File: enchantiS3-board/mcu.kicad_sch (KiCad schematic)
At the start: 7 parts, among them SW1 BOOT, SW2 ESP_RST

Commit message: Fixed BOM errors, removed unused Mounting Hole, added rev4 BOM
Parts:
- C2: Manufacturer Samsung Electro-Mechanics -> Murata Electronics; Mfg Part # CL05B104KO5NNNC -> GRM155R71C104KA88J
- C9: Manufacturer Samsung Electro-Mechanics -> Murata Electronics; Mfg Part # CL05A105KO5NNNC -> GRM155R61E105KA12D
- R5: Manufacturer Panasonic Electronic Components -> YAGEO; Mfg Part # ERJ-2RKF1002X -> RC0402FR-0710KL
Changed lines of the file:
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@@
 			)
 		)
-		(property "Description" "1 µF ±10% 16V Ceramic Capacitor X5R 0402 (1005 Metric)"
+		(property "Description" "1 µF ±10% 25V Ceramic Capacitor X5R 0402 (1005 Metric)"
 			(at 82.55 49.53 0)
 			(effects
@@
 			)
 		)
-		(property "Mfg Part #" "CL05A105KO5NNNC"
+		(property "Mfg Part #" "GRM155R61E105KA12D"
 			(at 82.55 49.53 0)
 			(effects
@@
 			)
 		)
-		(property "Manufacturer" "Samsung Electro-Mechanics"
+		(property "Manufacturer" "Murata Electronics"
 			(at 82.55 49.53 0)
 			(effects
@@
 			)
 		)
-		(property "Description" "10 kOhms ±1% 0.1W, 1/10W Chip Resistor 0402 (1005 Metric) Automotive AEC-Q200 Thick Film"
+		(property "Description" "10 kOhms ±1%  0.063W, 1/16W Chip Resistor 0402 (1005 Metric)"
 			(at 82.55 38.1 0)
 			(effects
@@
 			)
 		)
-		(property "Mfg Part #" "ERJ-2RKF1002X"
+		(property "Mfg Part #" "RC0402FR-0710KL"
 			(at 82.55 38.1 0)
 			(effects
@@
 			)
 		)
-		(property "Manufacturer" "Panasonic Electronic Components"
+		(property "Manufacturer" "YAGEO"
 			(at 82.55 38.1 0)
 			(effects
@@
 			)
 		)
-		(property "Mfg Part #" "CL05B104KO5NNNC"
+		(property "Mfg Part #" "GRM155R71C104KA88J"
 			(at 63.5 49.53 0)
 			(effects
@@
 			)
 		)
-		(property "Manufacturer" "Samsung Electro-Mechanics"
+		(property "Manufacturer" "Murata Electronics"
 			(at 63.5 49.53 0)
 			(effects

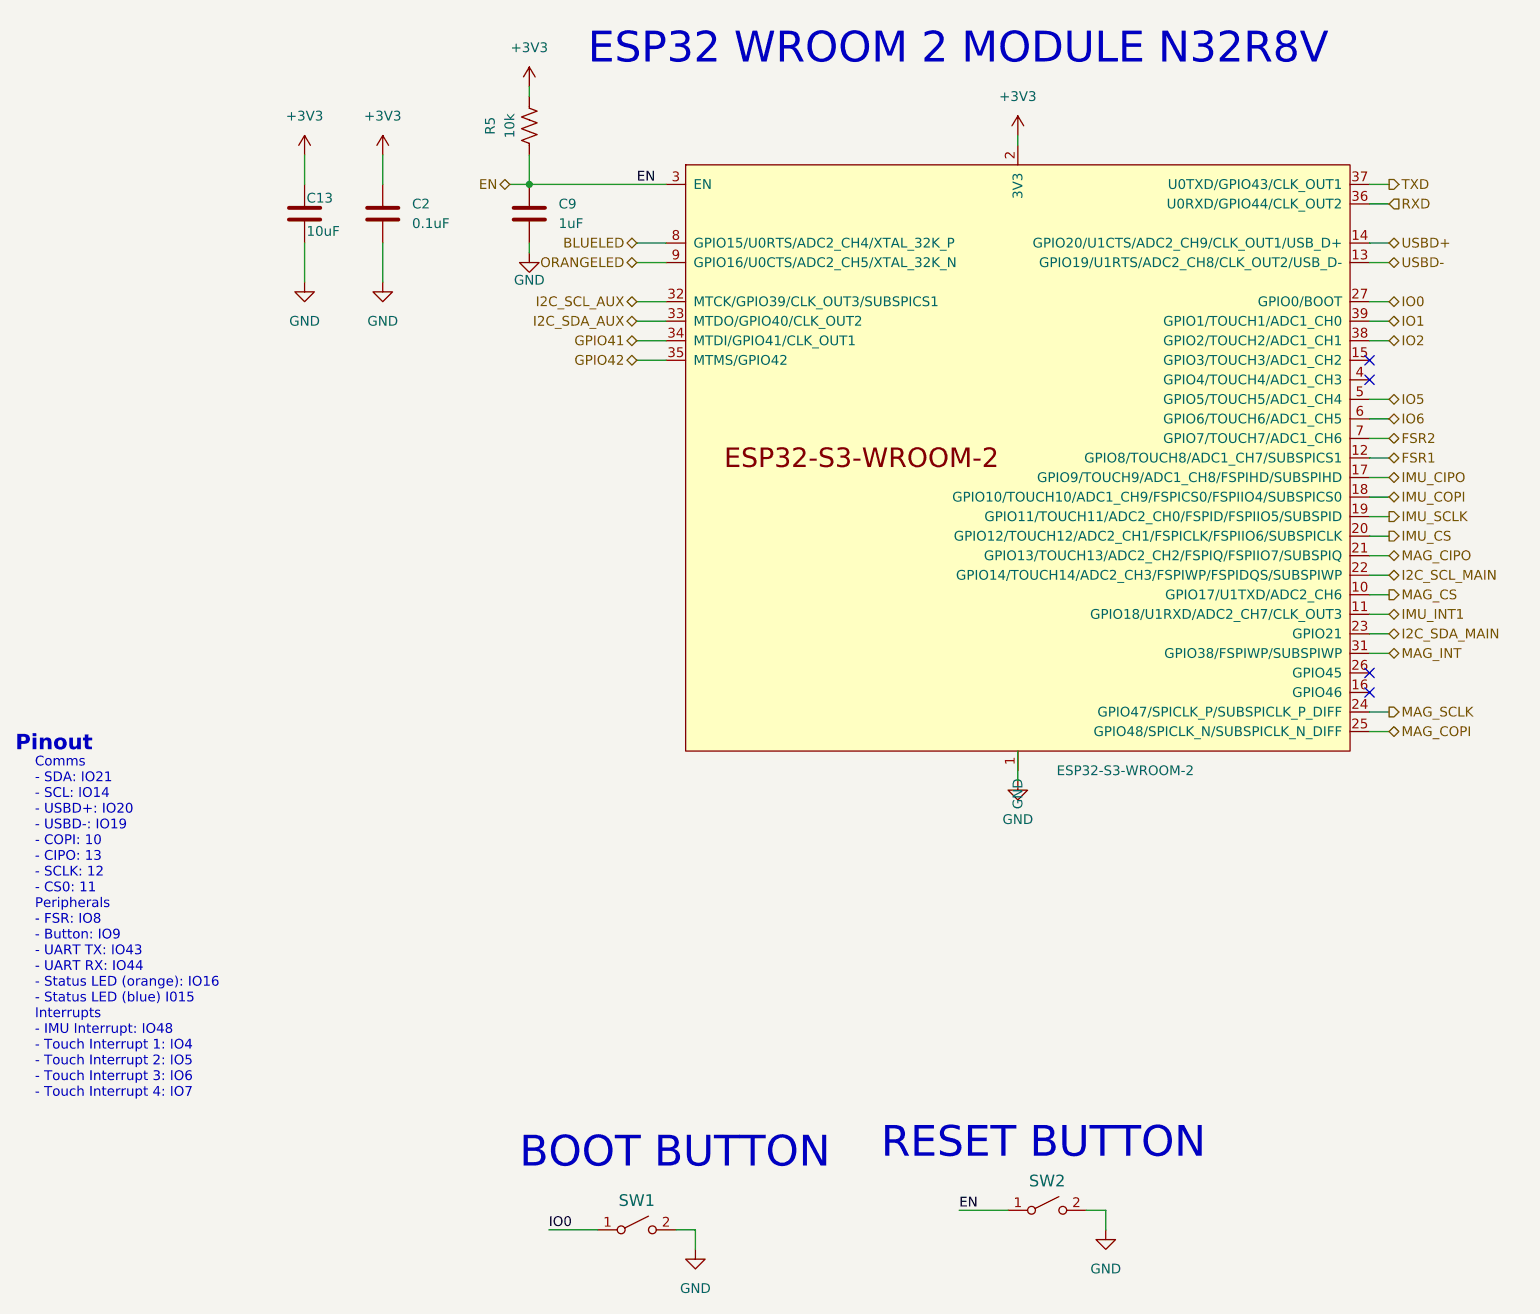
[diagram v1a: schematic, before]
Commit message: Switch to cheaper ESP32S3 WROOM 1 N8R8 Module
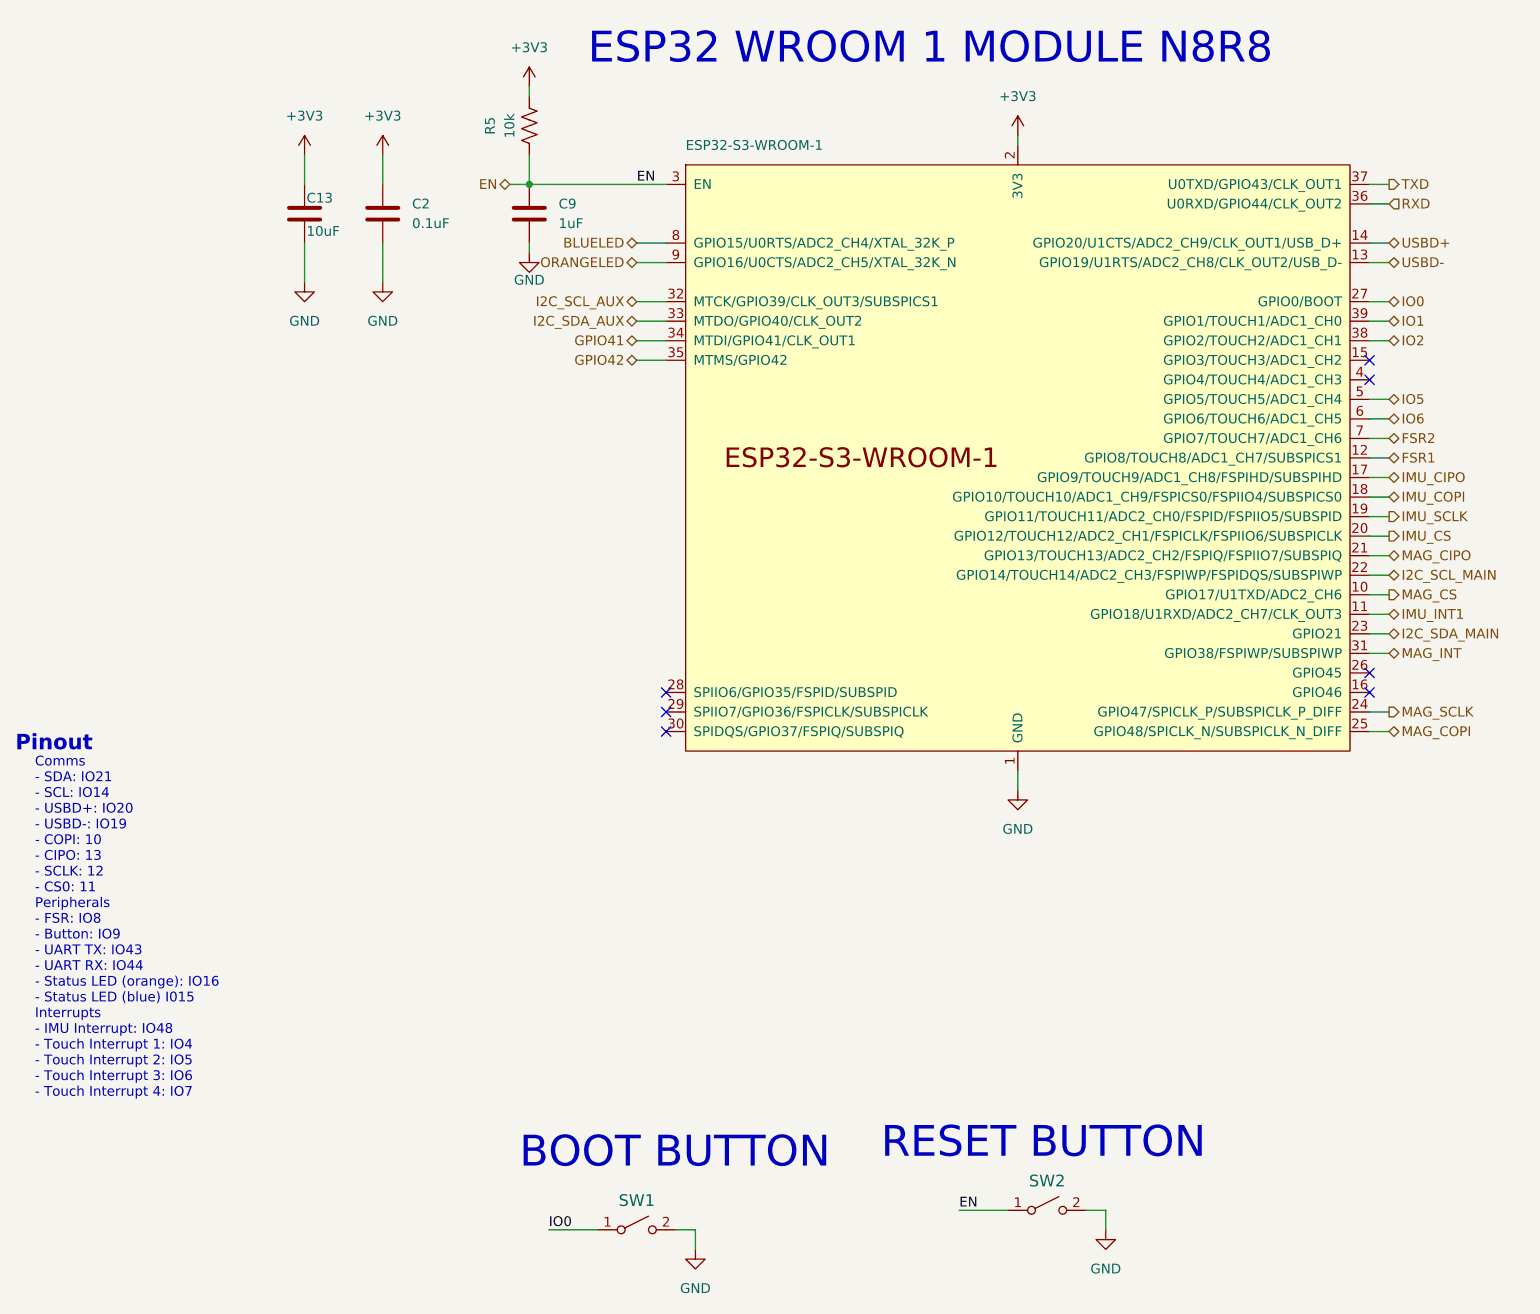
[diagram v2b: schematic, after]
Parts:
- MCU1: value ESP32-S3-WROOM-2 -> ESP32-S3-WROOM-1; footprint PCM_Espressif:ESP32-S3-WROOM-2 -> PCM_Espressif:ESP32-S3-WROOM-1; symbol PCM_Espressif:ESP32-S3-WROOM-2 -> PCM_Espressif:ESP32-S3-WROOM-1; Mfg Part # ESP32-S3-WROOM-2-N32R16V -> ESP32-S3-WROOM-1-N8R8
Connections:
- no-connect marks 4 -> 7
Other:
- note added: "ESP32 WROOM 1 MODULE N8R8"
- note removed: "ESP32 WROOM 2 MODULE N32R8V"
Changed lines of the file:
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@@
 		)
 	)
-	(text "ESP32 WROOM 2 MODULE N32R8V"
+	(text "ESP32 WROOM 1 MODULE N8R8"
 		(exclude_from_sim no)
 		(at 90.17 30.48 0)
@@
 	)
 	(no_connect
+		(at 100.33 114.3)
+	)
+	(no_connect
 		(at 191.77 68.58)
+	)
+	(no_connect
+		(at 100.33 111.76)
 	)
 	(no_connect
@@
 	)
 	(no_connect
+		(at 100.33 116.84)
+	)
+	(no_connect
 		(at 191.77 111.76)
 	)
@@
 	(wire
 		(pts
-			(xy 146.05 119.38) (xy 146.05 123.19)
+			(xy 146.05 121.92) (xy 146.05 124.46)
 		)
 		(stroke
@@
 		(lib_name "GND_2")
 		(lib_id "power:GND")
-		(at 146.05 123.19 0)
+		(at 146.05 124.46 0)
 		(unit 1)
 		(exclude_from_sim no)
@@
 		(fields_autoplaced yes)
 		(property "Reference" "#PWR0101"
+			(at 146.05 130.81 0)
+			(effects
+				(font
+					(size 1.27 1.27)
+				)
+				(hide yes)
+			)
+		)
+		(property "Value" "GND"
 			(at 146.05 129.54 0)
 			(effects
@@
 					(size 1.27 1.27)
 				)
-				(hide yes)
-			)
-		)
-		(property "Value" "GND"
-			(at 146.05 128.27 0)
-			(effects
-				(font
-					(size 1.27 1.27)
-				)
 			)
 		)
 		(property "Footprint" ""
-			(at 146.05 123.19 0)
+			(at 146.05 124.46 0)
 			(effects
 				(font
@@
 		)
 		(property "Datasheet" ""
-			(at 146.05 123.19 0)
+			(at 146.05 124.46 0)
 			(effects
 				(font
@@
 		)
 		(property "Description" ""
-			(at 146.05 123.19 0)
+			(at 146.05 124.46 0)
 			(effects
 				(font
@@
 	)
 	(symbol
-		(lib_id "PCM_Espressif:ESP32-S3-WROOM-2")
+		(lib_id "PCM_Espressif:ESP32-S3-WROOM-1")
 		(at 146.05 81.28 0)
 		(unit 1)
@@
 			)
 		)
-		(property "Value" "ESP32-S3-WROOM-2"
-			(at 160.02 121.92 0)
-			(effects
-				(font
-					(size 1.27 1.27)
-				)
-			)
-		)
-		(property "Footprint" "PCM_Espressif:ESP32-S3-WROOM-2"
+		(property "Value" "ESP32-S3-WROOM-1"
+			(at 102.87 40.64 0)
+			(effects
+				(font
+					(size 1.27 1.27)
+				)
+				(justify left)
+			)
+		)
+		(property "Footprint" "PCM_Espressif:ESP32-S3-WROOM-1"
 			(at 148.59 129.54 0)
 			(effects
@@
 			)
 		)
-		(property "Datasheet" "https://www.espressif.com/sites/default/files/documentation/esp32-s3-wroom-2_datasheet_en.pdf"
+		(property "Datasheet" "https://www.espressif.com/sites/default/files/documentation/esp32-s3-wroom-1_wroom-1u_datasheet_en.pdf"
 			(at 148.59 132.08 0)
 			(effects
@@
 			)
 		)
-		(property "Description" "Bluetooth, WiFi 802.11b/g/n, Bluetooth v5.0 Transceiver Module 2.4GHz PCB Trace Surface Mount"
+		(property "Description" "2.4 GHz WiFi (802.11 b/g/n) and Bluetooth ® 5 (LE) module Built around ESP32S3 series of SoCs, Xtensa ® dualcore 32bit LX7 microprocessor Flash up to 16 MB, PSRAM up to 8 MB 36 GPIOs, rich set of peripherals Onboard PCB antenna"
 			(at 146.05 81.28 0)
 			(effects
@@
 			)
 		)
-		(property "Mfg Part #" "ESP32-S3-WROOM-2-N32R16V"
+		(property "Mfg Part #" "ESP32-S3-WROOM-1-N8R8"
 			(at 146.05 81.28 0)
 			(effects
